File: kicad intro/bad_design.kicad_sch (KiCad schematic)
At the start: 13 parts, among them J1 USB_C_Receptacle_PowerOnly_6P, J2 Conn_01x03_Socket, J3 Conn_01x03_Socket, Q1 BF459, U1 ATtiny85-20P

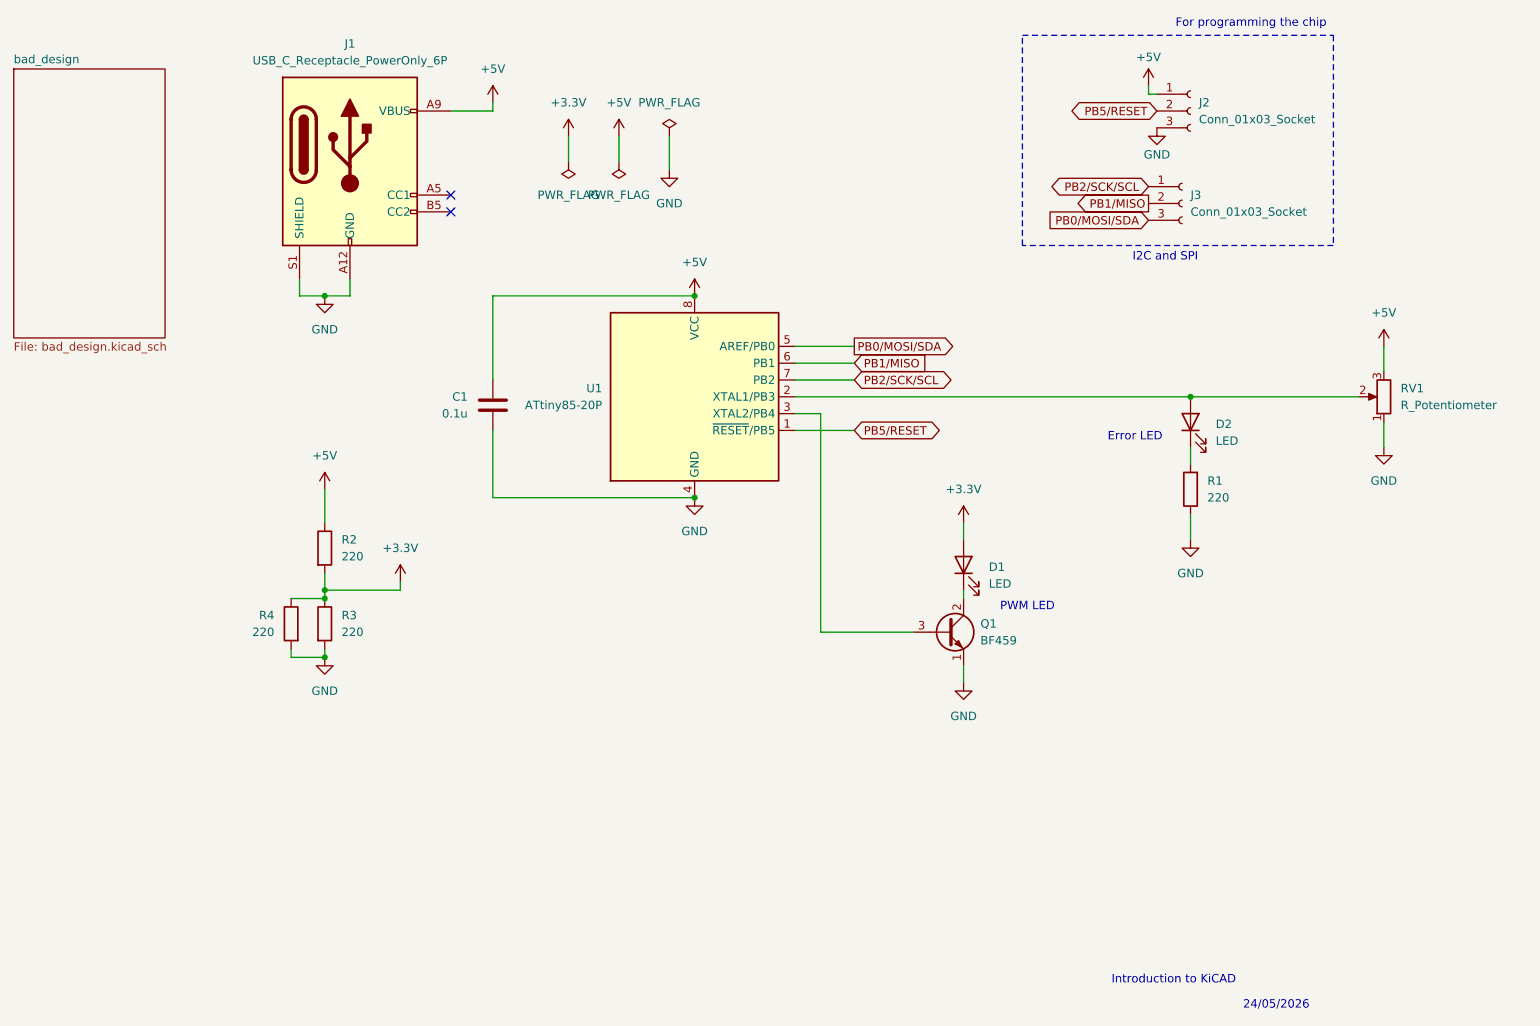
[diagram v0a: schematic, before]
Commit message: added examples of bad design
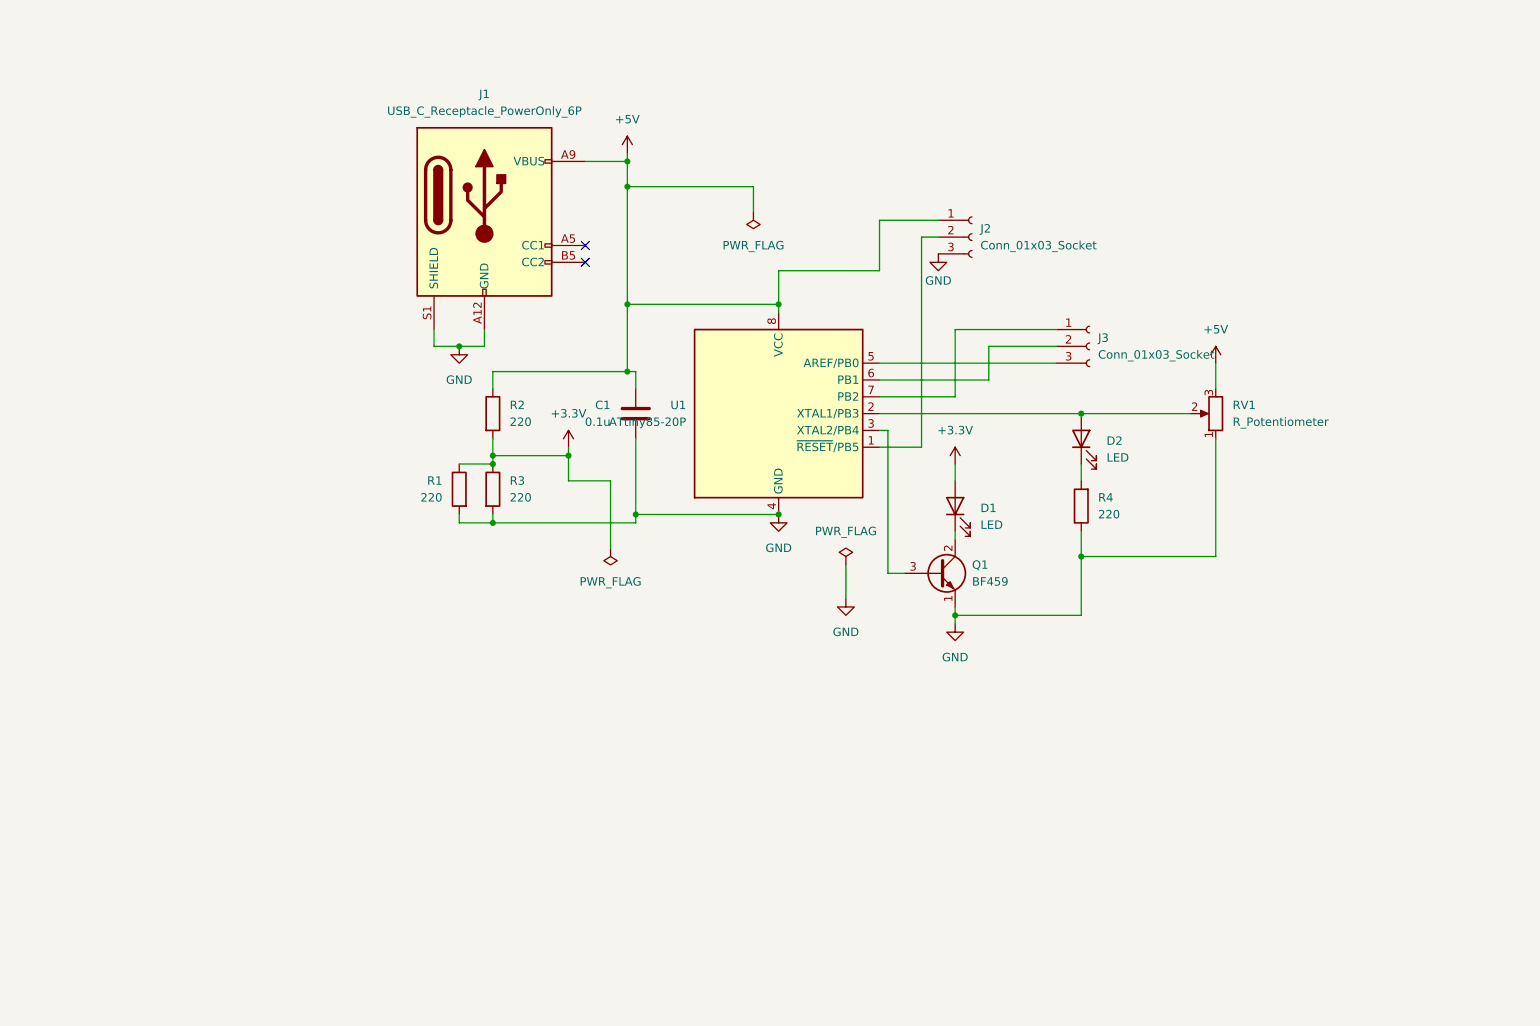
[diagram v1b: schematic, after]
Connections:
- net +3.3V: now also R1.1; no longer R4.1
- net GND: now also R1.2, R4.1; no longer R1.1, R4.2
- net at D2.1 (K): now also R4.2; no longer R1.2
- net PB0/MOSI/SDA: no longer names the net of J3.3 (Pin_3), U1.5 (AREF/PB0)
- net PB1/MISO: no longer names the net of J3.2 (Pin_2), U1.6 (PB1)
- net PB2/SCK/SCL: no longer names the net of J3.1 (Pin_1), U1.7 (PB2)
- net PB5/RESET: no longer names the net of J2.2 (Pin_2), U1.1 (~{RESET}/PB5)
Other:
- removed sheet bad_design
- note removed: "24/05/2026"
- note removed: "Error LED"
- note removed: "For programming the chip"
- note removed: "I2C and SPI"
- note removed: "Introduction to KiCAD"
- note removed: "PWM LED"

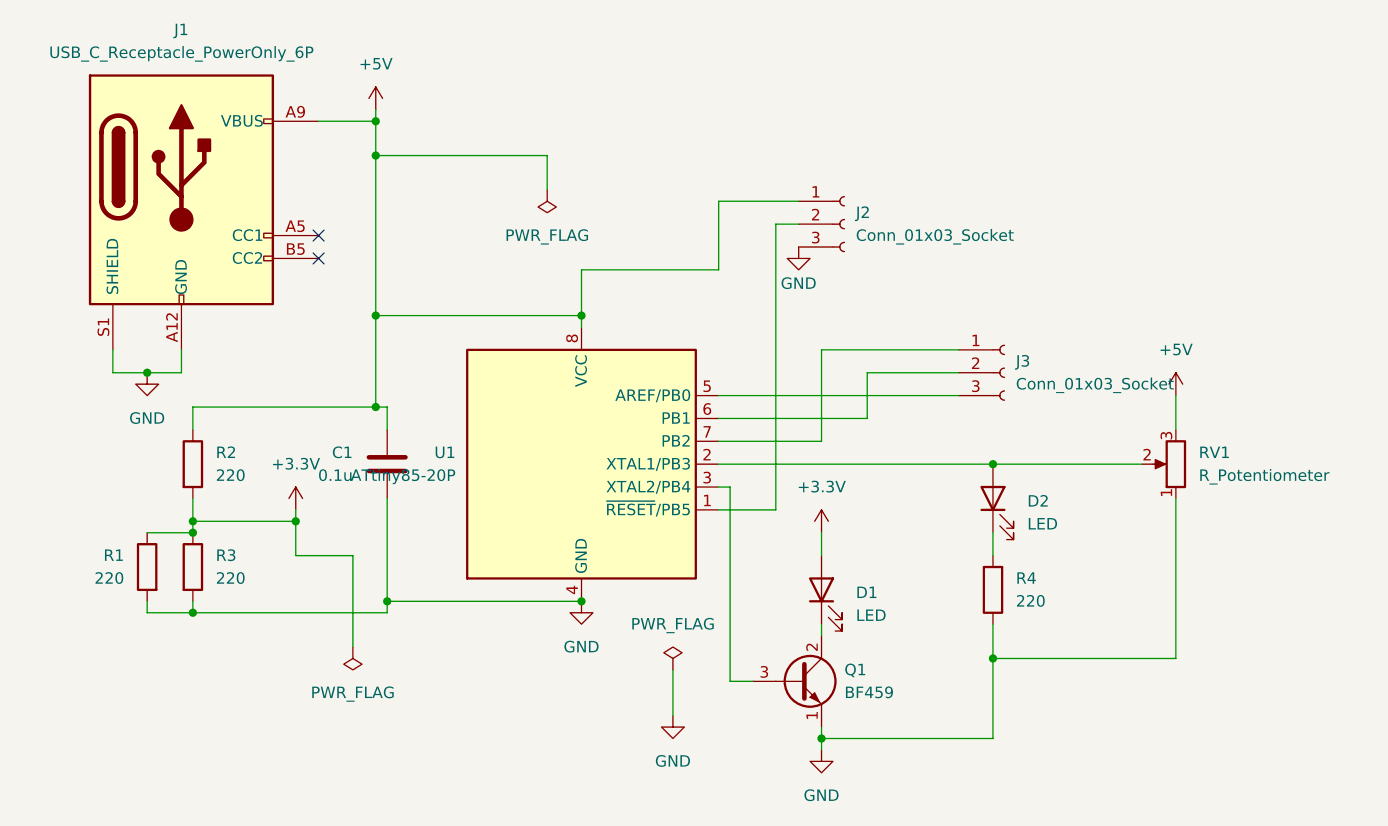
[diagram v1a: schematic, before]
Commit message: Separated ground pours
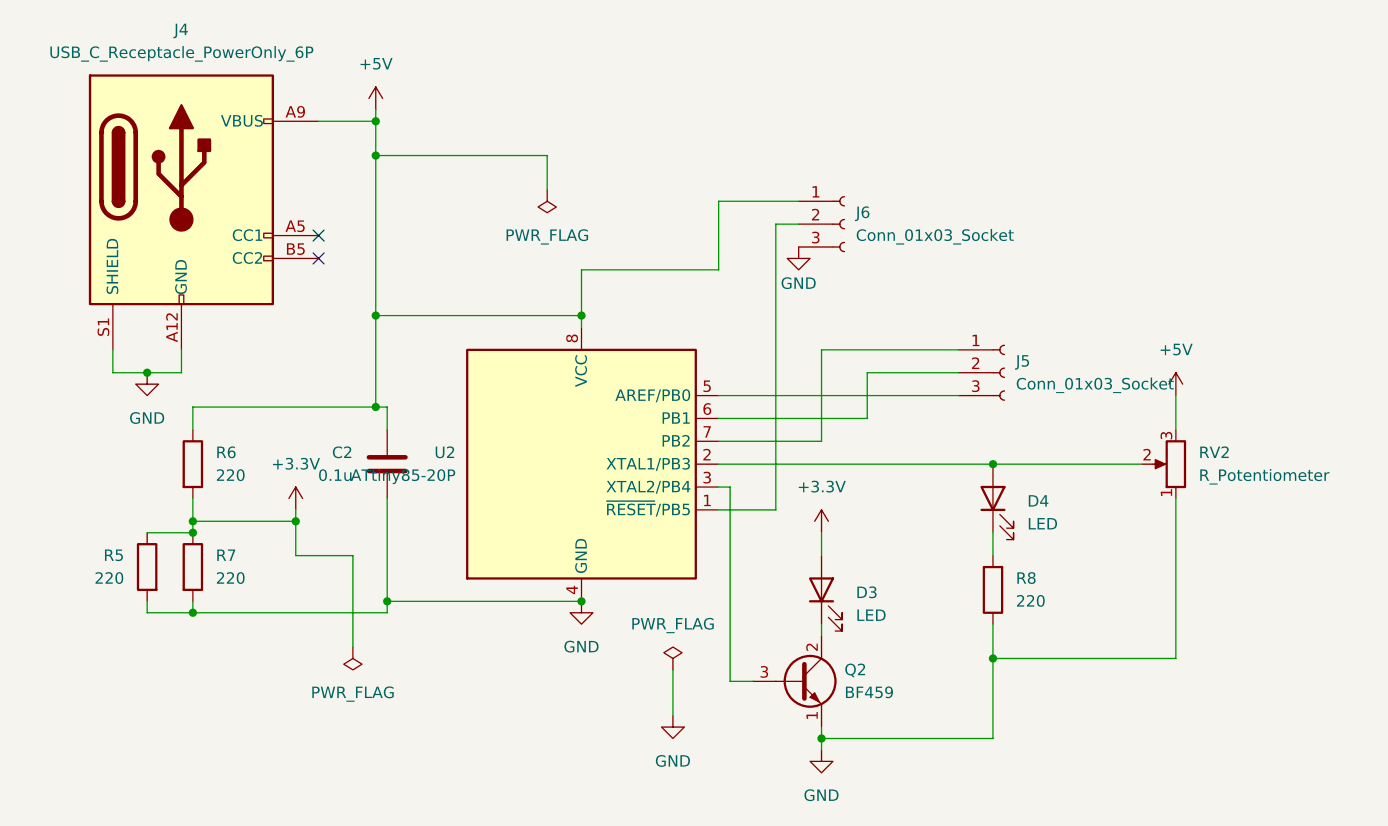
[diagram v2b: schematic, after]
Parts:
- renumbered C1 to C2, D1 to D3, D2 to D4, J1 to J4, J3 to J5, J2 to J6, Q1 to Q2, R1 to R5, R2 to R6, R3 to R7, R4 to R8, RV1 to RV2, U1 to U2
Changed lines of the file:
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@@
 		(dnp no)
 		(fields_autoplaced yes)
-		(property "Reference" "R4"
+		(property "Reference" "R8"
 			(at 186.69 116.8399 0)
 			(effects
@@
 		(dnp no)
 		(fields_autoplaced yes)
-		(property "Reference" "#PWR03"
+		(property "Reference" "#PWR022"
 			(at 115.57 68.58 0)
 			(effects
@@
 		(dnp no)
 		(fields_autoplaced yes)
-		(property "Reference" "#PWR07"
+		(property "Reference" "#PWR028"
 			(at 165.1 115.57 0)
 			(effects
@@
 		(dnp no)
 		(fields_autoplaced yes)
-		(property "Reference" "#FLG01"
+		(property "Reference" "#FLG04"
 			(at 113.03 126.365 0)
 			(effects
@@
 		(on_board yes)
 		(dnp no)
-		(property "Reference" "C1"
+		(property "Reference" "C2"
 			(at 113.03 102.8699 0)
 			(effects
@@
 		(on_board yes)
 		(dnp no)
-		(property "Reference" "#PWR06"
+		(property "Reference" "#PWR031"
 			(at 162.56 86.36 0)
 			(effects
@@
 		(dnp no)
 		(fields_autoplaced yes)
-		(property "Reference" "D1"
+		(property "Reference" "D3"
 			(at 168.91 118.4274 90)
 			(effects
@@
 		(dnp no)
 		(fields_autoplaced yes)
-		(property "Reference" "#PWR05"
+		(property "Reference" "#PWR025"
 			(at 148.59 138.43 0)
 			(effects
@@
 		(dnp no)
 		(fields_autoplaced yes)
-		(property "Reference" "R2"
+		(property "Reference" "R6"
 			(at 97.79 102.8699 0)
 			(effects
@@
 		(dnp no)
 		(fields_autoplaced yes)
-		(property "Reference" "#PWR08"
+		(property "Reference" "#PWR029"
 			(at 165.1 142.24 0)
 			(effects
@@
 		(dnp no)
 		(fields_autoplaced yes)
-		(property "Reference" "J1"
+		(property "Reference" "J4"
 			(at 93.98 55.88 0)
 			(effects
@@
 		(dnp no)
 		(fields_autoplaced yes)
-		(property "Reference" "#PWR02"
+		(property "Reference" "#PWR021"
 			(at 106.68 113.03 0)
 			(effects
@@
 		(on_board yes)
 		(dnp no)
-		(property "Reference" "R1"
+		(property "Reference" "R5"
 			(at 87.63 114.2999 0)
 			(effects
@@
 		(dnp no)
 		(fields_autoplaced yes)
-		(property "Reference" "J3"
+		(property "Reference" "J5"
 			(at 186.69 92.7099 0)
 			(effects
@@
 		(dnp no)
 		(fields_autoplaced yes)
-		(property "Reference" "J2"
+		(property "Reference" "J6"
 			(at 168.91 76.1999 0)
 			(effects
@@
 		(on_board yes)
 		(dnp no)
-		(property "Reference" "#FLG02"
+		(property "Reference" "#FLG05"
 			(at 134.62 75.565 0)
 			(effects
@@
 		(dnp no)
 		(fields_autoplaced yes)
-		(property "Reference" "R3"
+		(property "Reference" "R7"
 			(at 97.79 114.2999 0)
 			(effects
@@
 		(dnp no)
 		(fields_autoplaced yes)
-		(property "Reference" "#FLG03"
+		(property "Reference" "#FLG06"
 			(at 148.59 125.095 0)
 			(effects
@@
 		(dnp no)
 		(fields_autoplaced yes)
-		(property "Reference" "D2"
+		(property "Reference" "D4"
 			(at 187.96 108.2674 90)
 			(effects
@@
 		(dnp no)
 		(fields_autoplaced yes)
-		(property "Reference" "#PWR01"
+		(property "Reference" "#PWR018"
 			(at 90.17 100.33 0)
 			(effects
@@
 		(dnp no)
 		(fields_autoplaced yes)
-		(property "Reference" "U1"
+		(property "Reference" "U2"
 			(at 124.46 102.8699 0)
 			(effects
@@
 		(dnp no)
 		(fields_autoplaced yes)
-		(property "Reference" "RV1"
+		(property "Reference" "RV2"
 			(at 207.01 102.8699 0)
 			(effects
@@
 		(dnp no)
 		(fields_autoplaced yes)
-		(property "Reference" "#PWR04"
+		(property "Reference" "#PWR027"
 			(at 138.43 125.73 0)
 			(effects
@@
 		(dnp no)
 		(fields_autoplaced yes)
-		(property "Reference" "#PWR09"
+		(property "Reference" "#PWR033"
 			(at 204.47 100.33 0)
 			(effects
@@
 		(dnp no)
 		(fields_autoplaced yes)
-		(property "Reference" "Q1"
+		(property "Reference" "Q2"
 			(at 167.64 126.9999 0)
 			(effects
